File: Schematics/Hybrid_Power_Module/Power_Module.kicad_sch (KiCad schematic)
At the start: 0 parts

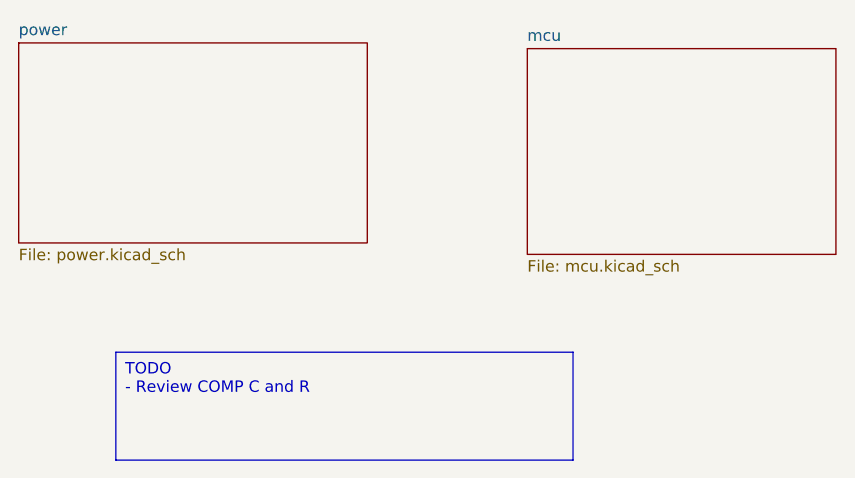
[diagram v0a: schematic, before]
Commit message: fix: Updates after testing, for next revision
 - add current limiting to GSE RPP zener shunt
 - switched 5v current sensor
 - flipped CAN and UART polarity
 - add 3.3v reference to CAN transceiver
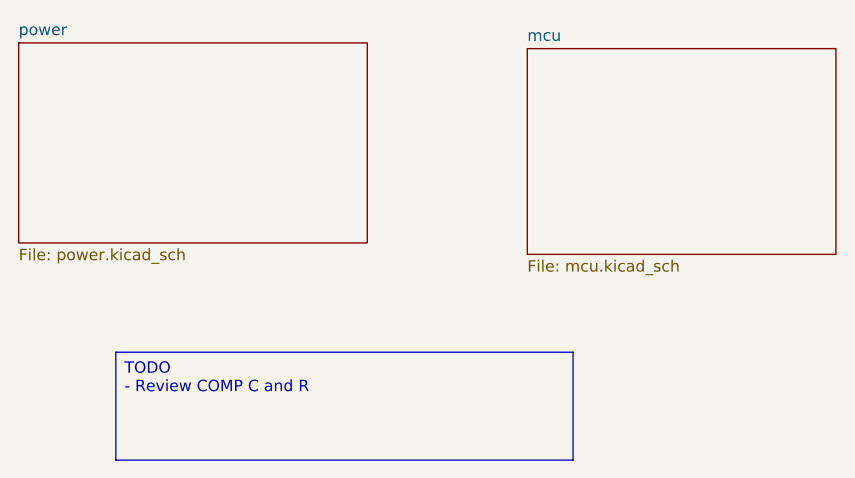
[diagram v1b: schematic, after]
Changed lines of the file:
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@@
 (kicad_sch
-	(version 20231120)
+	(version 20260306)
 	(generator "eeschema")
-	(generator_version "8.0")
+	(generator_version "10.0")
 	(paper "A4")
 	(title_block
@@
 		(at 113.03 115.0112 0)
 		(size 50.8 11.9888)
+		(margins 0.9525 0.9525 0.9525 0.9525)
 		(stroke
 			(width 0)
@@
 		(at 158.75 81.28)
 		(size 34.29 22.86)
+		(exclude_from_sim no)
+		(in_bom yes)
+		(on_board yes)
+		(dnp no)
 		(fields_autoplaced yes)
 		(stroke
@@
 		)
 		(fill
-			(color 0 0 0 0.0000)
+			(color 0 0 0 0)
 		)
 		(property "Sheetname" "mcu"
 			(at 158.75 80.5684 0)
+			(show_name no)
+			(do_not_autoplace no)
 			(effects
 				(font
@@
 		(property "Sheetfile" "mcu.kicad_sch"
 			(at 158.75 104.7246 0)
+			(show_name no)
+			(do_not_autoplace no)
 			(effects
 				(font
@@
 		(at 102.235 80.645)
 		(size 38.735 22.225)
+		(exclude_from_sim no)
+		(in_bom yes)
+		(on_board yes)
+		(dnp no)
 		(fields_autoplaced yes)
 		(stroke
@@
 		)
 		(fill
-			(color 0 0 0 0.0000)
+			(color 0 0 0 0)
 		)
 		(property "Sheetname" "power"
 			(at 102.235 79.9334 0)
+			(show_name no)
+			(do_not_autoplace no)
 			(effects
 				(font
@@
 		(property "Sheetfile" "power.kicad_sch"
 			(at 102.235 103.4546 0)
+			(show_name no)
+			(do_not_autoplace no)
 			(effects
 				(font
@@
 		)
 	)
+	(embedded_fonts no)
 )
